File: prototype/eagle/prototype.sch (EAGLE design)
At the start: 37 parts, among them T1 3904, U1 ARDUINO_MINI_PRO, U2 ATA6631, U4 FTDI-BOARD

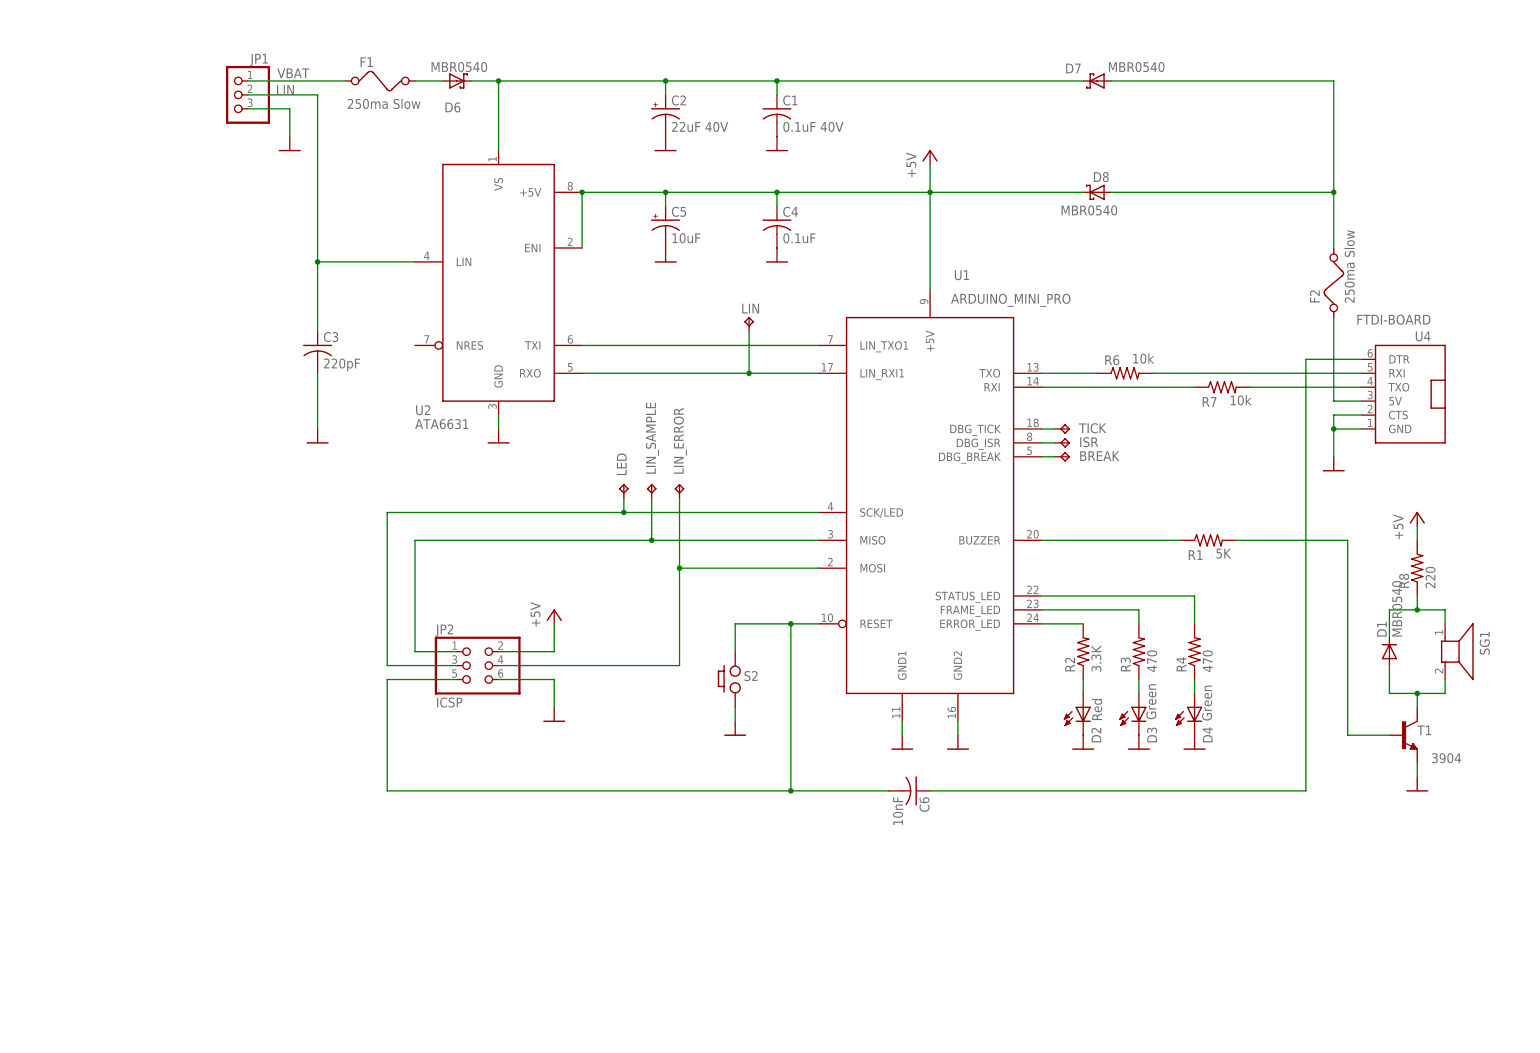
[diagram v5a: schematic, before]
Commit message: Added a second lin interface for the slave.
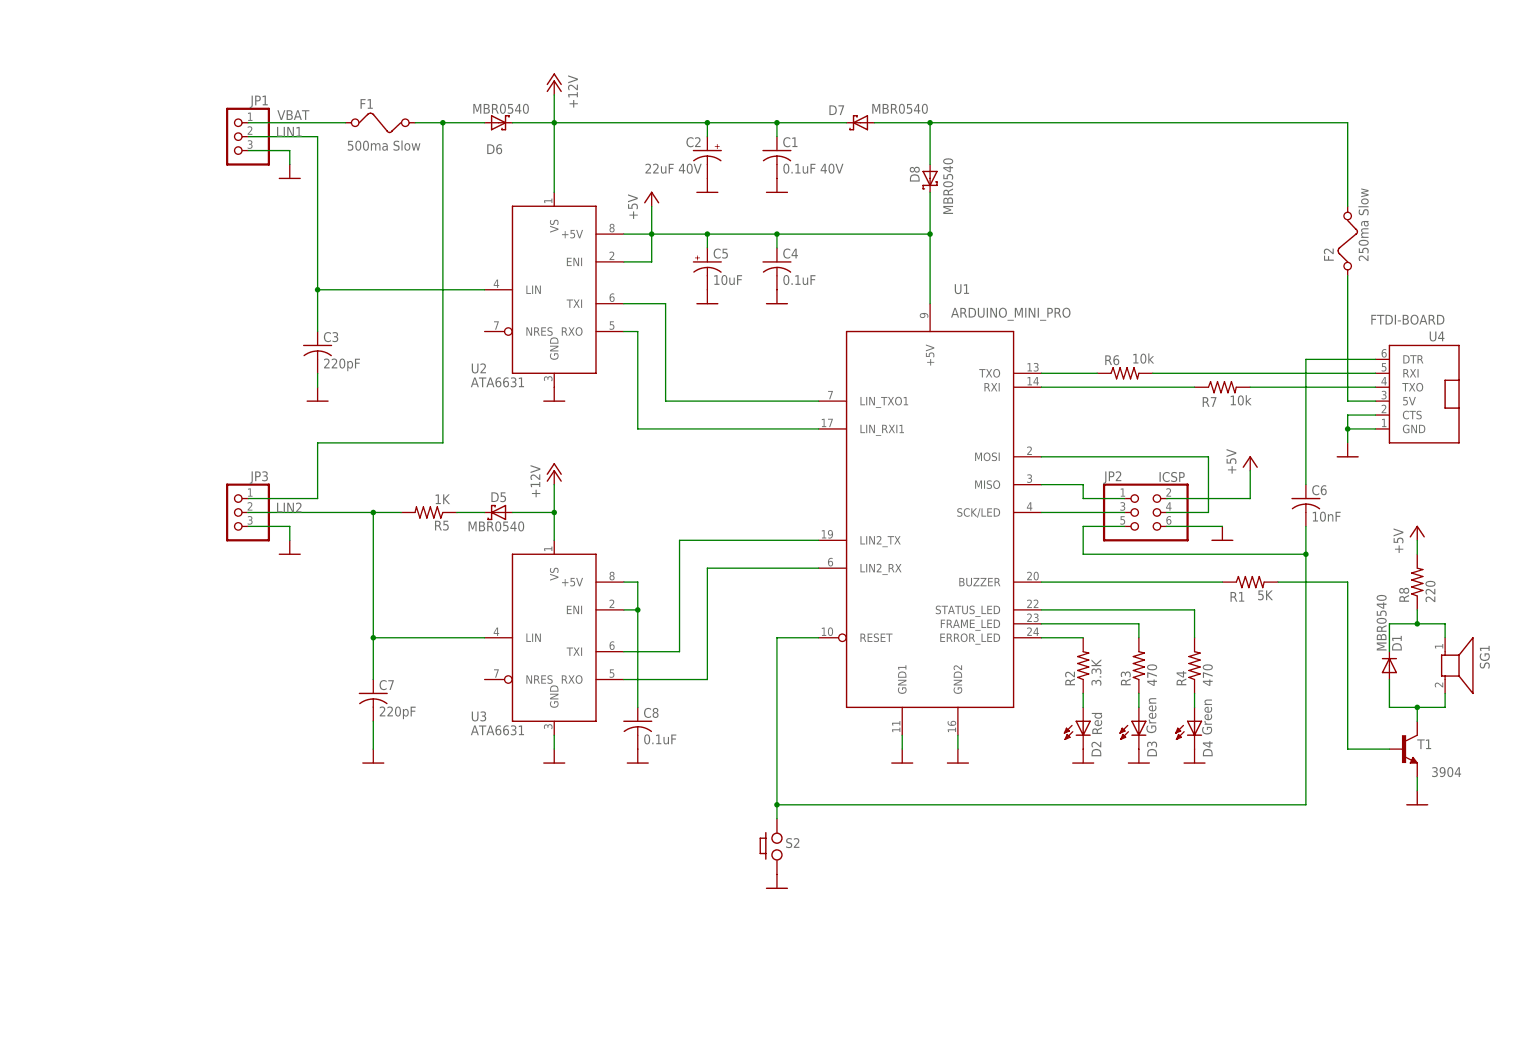
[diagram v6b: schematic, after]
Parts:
- removed BREAK, ISR, LED, LIN, LIN_ERROR, LIN_SAMPLE, TICK: TPPAD1-17, testpad:TPPAD1-17
- added C7: 220pF, rcl:C-USC0805
- added C8: 0.1uF, rcl:C-USC0805
- added D5: MBR0540, diode:MBRS320T3
- added JP3: (no value), pinhead:PINHD-1X3
- added R5: 1K, rcl:R-US_R0805
- added U3: ATA6631, prototype:ATA6631
- F1: value 250ma Slow -> 500ma Slow
- U2: device beeper:ATA6631 -> prototype:ATA6631
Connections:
- net LIN renamed LIN1
- removed net N$24: D6.A, F1.2
- removed net N$26: TICK.TP, U1.DBG_TICK
- removed net N$29: ISR.TP, U1.DBG_ISR
- removed net N$5 (its old number): BREAK.TP, U1.DBG_BREAK
- new net LIN2: C7.1, JP3.2, R5.2, U3.LIN
- new net N$10: U1.LIN2_TX, U3.TXI
- new net N$11: U1.LIN2_RX, U3.RXO
- new net N$15: D5.C, R5.1
- new net N$6: D6.A, F1.2, JP3.1
- net +12V: now also D5.A, U3.VS
- net +5V: now also C8.1, U3.+5V, U3.ENI
- net GND: now also C7.2, C8.2, JP3.3, U3.GND
- net N$18: no longer LIN.TP
- net N$20: no longer LIN_ERROR.TP
- net N$25: no longer LIN_SAMPLE.TP
- net N$28: no longer LED.TP
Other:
- moved on the sheet: C1, C2, C4, C5, C6, D1, D2, D3, D4, D6, D7, D8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

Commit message: Changed the prototype schematic to use a raw atmega328 instead of Arduino Pro Mini.
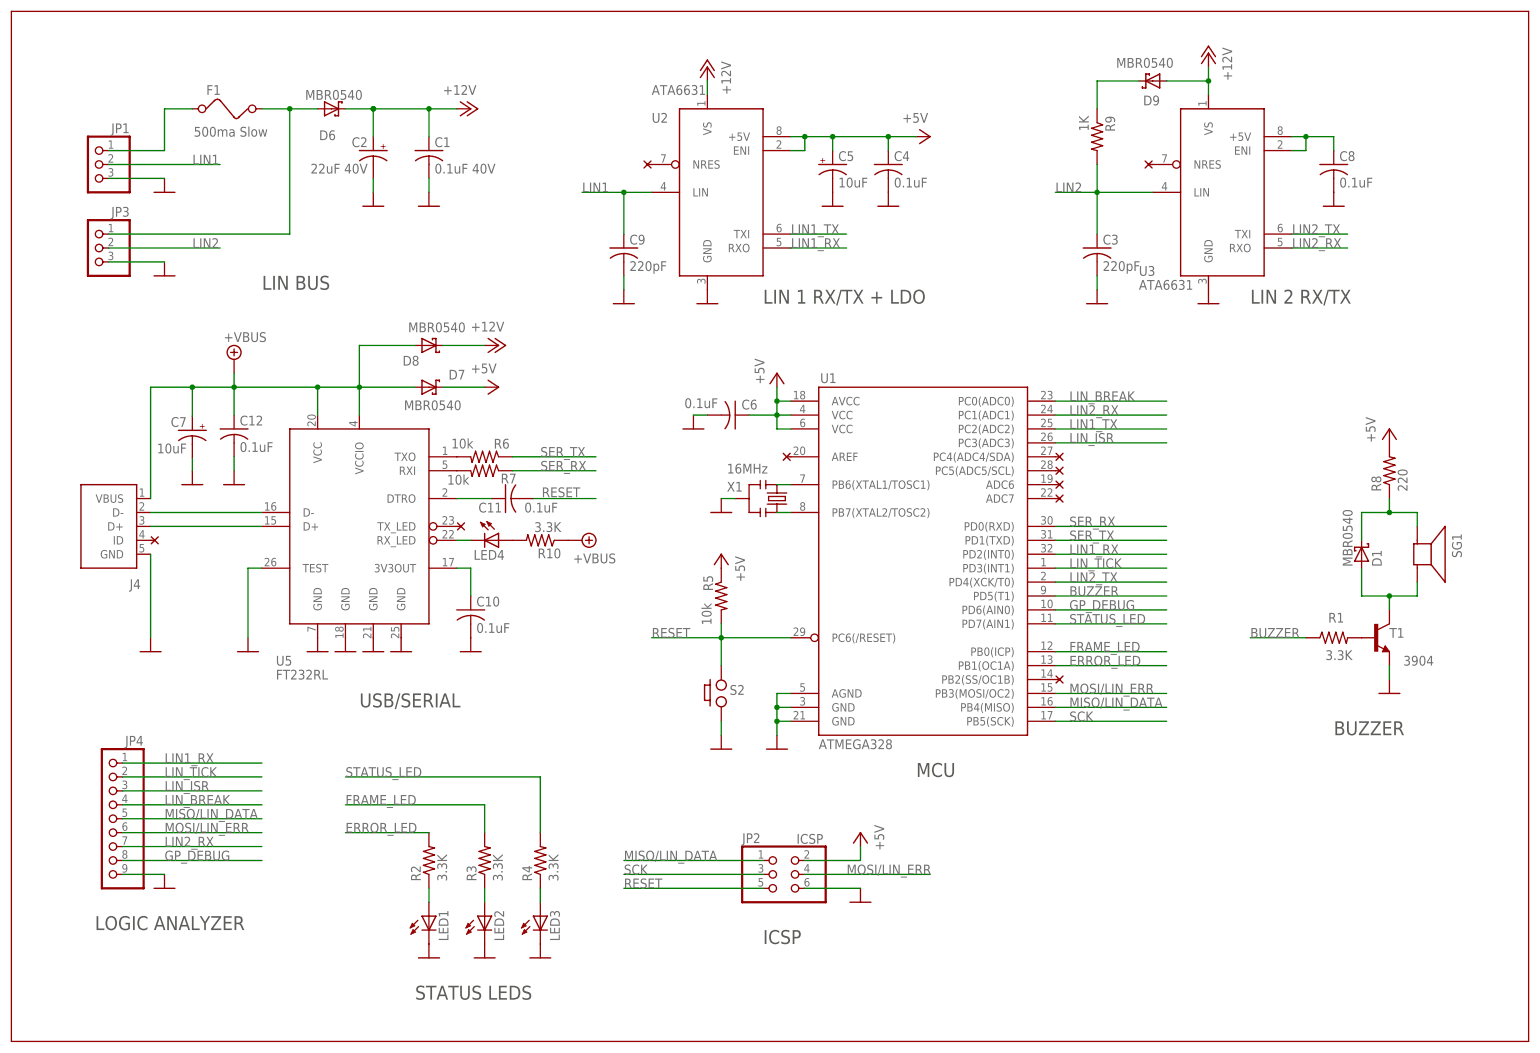
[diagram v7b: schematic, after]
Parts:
- removed D2: Red, display-hp:HLMP6
- removed D3, D4: Green, display-hp:HLMP6
- removed D5: MBR0540, diode:MBRS320T3
- removed F2: 250ma Slow, special:FUSE
- removed U4: FTDI-BOARD, prototype:FTDI-OBARD
- added C10, C11, C12: 0.1uF, prototype:C-USC0805
- added C9: 220pF, prototype:C-USC0805
- added D9: MBR0540, prototype:SMF5.0AT1
- added J4: USBSMD, prototype:USBSMD
- added JP4: (no value), prototype:PINHD-1X9
- added LED1, LED2, LED3, LED4: (no value), prototype:LED
- added R10: 3.3K, prototype:R-US_R0805
- added R9: 1K, prototype:R-US_R0805
- added U5: FT232RL, prototype:FT232RL
- added X1: 16MHz, prototype:RESONATORSMD
- C1, C3, C4, C8: device rcl:C-USC0805 -> prototype:C-USC0805
- C2: device rcl:CPOL-USSMCC -> prototype:CPOL-USUD-6,3X5,8
- C5: device rcl:CPOL-USSMCC -> prototype:CPOL-USA/3216-18R
- C6: value 10nF -> 0.1uF; device rcl:C-USC0805 -> prototype:C-USC0805
- C7: value 220pF -> 10uF; device rcl:C-USC0805 -> prototype:CPOL-USA/3216-18R
- D1: device diode:DIODE-MINIMELF -> prototype:SMF5.0AT1
- D6, D7, D8: device diode:MBRS320T3 -> prototype:SMF5.0AT1
- F1: device special:FUSE -> prototype:FUSE
- JP1, JP3: device pinhead:PINHD-1X3 -> prototype:PINHD-1X3
- JP2: device pinhead:PINHD-2X3 -> prototype:PINHD-2X3
- R1: value 5K -> 3.3K; device rcl:R-US_R0805 -> prototype:R-US_R0805
- R2, R6, R7, R8: device rcl:R-US_R0805 -> prototype:R-US_R0805
- R3, R4: value 470 -> 3.3K; device rcl:R-US_R0805 -> prototype:R-US_R0805
- R5: value 1K -> 10k; device rcl:R-US_R0805 -> prototype:R-US_R0805
- SG1: value F/SMX -> AL60P; device buzzer:F/SMX -> prototype:AL60P
- T1: device transistor:MMBT3904LT1-NPN-SOT23-BEC -> prototype:MMBT3904LT1-NPN-SOT23-BEC
- U1: value ARDUINO_MINI_PRO -> ATMEGA328; device prototype:ARDUINO_MINI_PRODIP24-6 -> prototype:ATMEGA328
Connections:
- removed net N$10: U1.LIN2_TX, U3.TXI
- removed net N$11: U1.LIN2_RX, U3.RXO
- removed net N$13: C6.1, U4.DTR
- removed net N$17: R1.1, U1.BUZZER
- removed net N$18: U1.LIN_RXI1, U2.RXO
- removed net N$20: JP2.4, U1.MOSI
- removed net N$21: R7.2, U4.TXO
- removed net N$23: R6.2, U4.RXI
- removed net N$25: JP2.1, U1.MISO
- removed net N$28: JP2.3, U1.SCK/LED
- removed net N$5: C6.2, JP2.5, S2.P$3, U1.RESET
- new net +VBUS: C12.1, C7.+, D7.A, D8.A, J4.VBUS, R10.1, U5.VCC, U5.VCCIO
- new net BUZZER: R1.1, U1.PD5(T1)
- new net ERROR_LED: R2.2, U1.PB1(OC1A)
- new net FRAME_LED: R3.2, U1.PB0(ICP)
- new net GP_DEBUG: JP4.8, U1.PD6(AIN0)
- new net LIN1_RX: JP4.1, U1.PD2(INT0), U2.RXO
- new net LIN1_TX: U1.PC2(ADC2), U2.TXI
- new net LIN2_RX: JP4.7, U1.PC1(ADC1), U3.RXO
- new net LIN2_TX: U1.PD4(XCK/T0), U3.TXI
- new net LIN_BREAK: JP4.4, U1.PC0(ADC0)
- new net LIN_ISR: JP4.3, U1.PC3(ADC3)
- new net LIN_TICK: JP4.2, U1.PD3(INT1)
- new net MISO/LIN_DATA: JP2.1, JP4.5, U1.PB4(MISO)
- new net MOSI/LIN_ERR: JP2.4, JP4.6, U1.PB3(MOSI/OC2)
- new net RESET: C11.2, JP2.5, R5.2, S2.P$3, U1.PC6(/RESET)
- new net SCK: JP2.3, U1.PB5(SCK)
- new net SECONDARY_5V: C8.1, U3.+5V, U3.ENI
- new net SER_RX: R7.1, U1.PD0(RXD)
- new net SER_TX: R6.1, U1.PD1(TXD)
- new net STATUS_LED: R4.2, U1.PD7(AIN1)
- new net XTAL1: U1.PB6(XTAL1/TOSC1), X1.3
- new net XTAL2: U1.PB7(XTAL2/TOSC2), X1.1
- net +12V: now also D8.C, D9.A; no longer D5.A, D7.C
- net +5V: now also C6.1, D7.C, R5.1, U1.AVCC, U1.VCC@1, U1.VCC@2; no longer C8.1, D8.C, U1.+5V, U3.+5V, U3.ENI
- net GND: now also C10.2, C12.2, C6.2, C7.-, C9.2, J4.GND, JP4.9, LED1.C, LED2.C, LED3.C, U1.AGND, U1.GND@1, U1.GND@2, U5.GND@1, U5.GND@2, U5.GND@3, U5.GND@4, U5.TEST, X1.2; no longer C7.2, D2.K, D3.K, D4.K, U1.GND1, U1.GND2, U4.CTS, U4.GND
- net LIN1: now also C9.1; no longer C3.1
- net LIN2: now also C3.1, R9.2; no longer C7.1, R5.2
- net N$1: now also LED4.C, U5.RX_LED; no longer U1.LIN_TXO1, U2.TXI
- net N$12: now also R6.2, U5.TXO; no longer D7.A, D8.A, F2.2
- net N$14: now also C11.1, U5.DTRO; no longer R7.1, U1.RXI
- net N$15: now also LED4.A, R10.2; no longer D5.C, R5.1
- net N$16: now also R7.2, U5.RXI; no longer F2.1, U4.5V
- net N$2: now also LED3.A; no longer D4.A
- net N$22: now also C10.1, U5.3V3OUT; no longer R6.1, U1.TXO
- net N$3: now also LED2.A; no longer D3.A
- net N$4: now also LED1.A; no longer D2.A
- net N$7: now also J4.D+, U5.D+; no longer R2.2, U1.ERROR_LED
- net N$8: now also J4.D-, U5.D-; no longer R3.2, U1.FRAME_LED
- net N$9: now also D9.C, R9.1; no longer R4.2, U1.STATUS_LED
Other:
- note added: "BUZZER"
- note added: "ICSP"
- note added: "LIN 1 RX/TX + LDO"
- note added: "LIN 2 RX/TX"
- note added: "LIN BUS"
- note added: "LOGIC ANALYZER"
- note added: "MCU"
- note added: "STATUS LEDS"
- note added: "USB/SERIAL"
- moved on the sheet: D6, D7, D8, F1, JP1, JP2, JP3, R1, R2, R3, R4, R5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
